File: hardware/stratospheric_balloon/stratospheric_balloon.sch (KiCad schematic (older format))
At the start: 6 parts

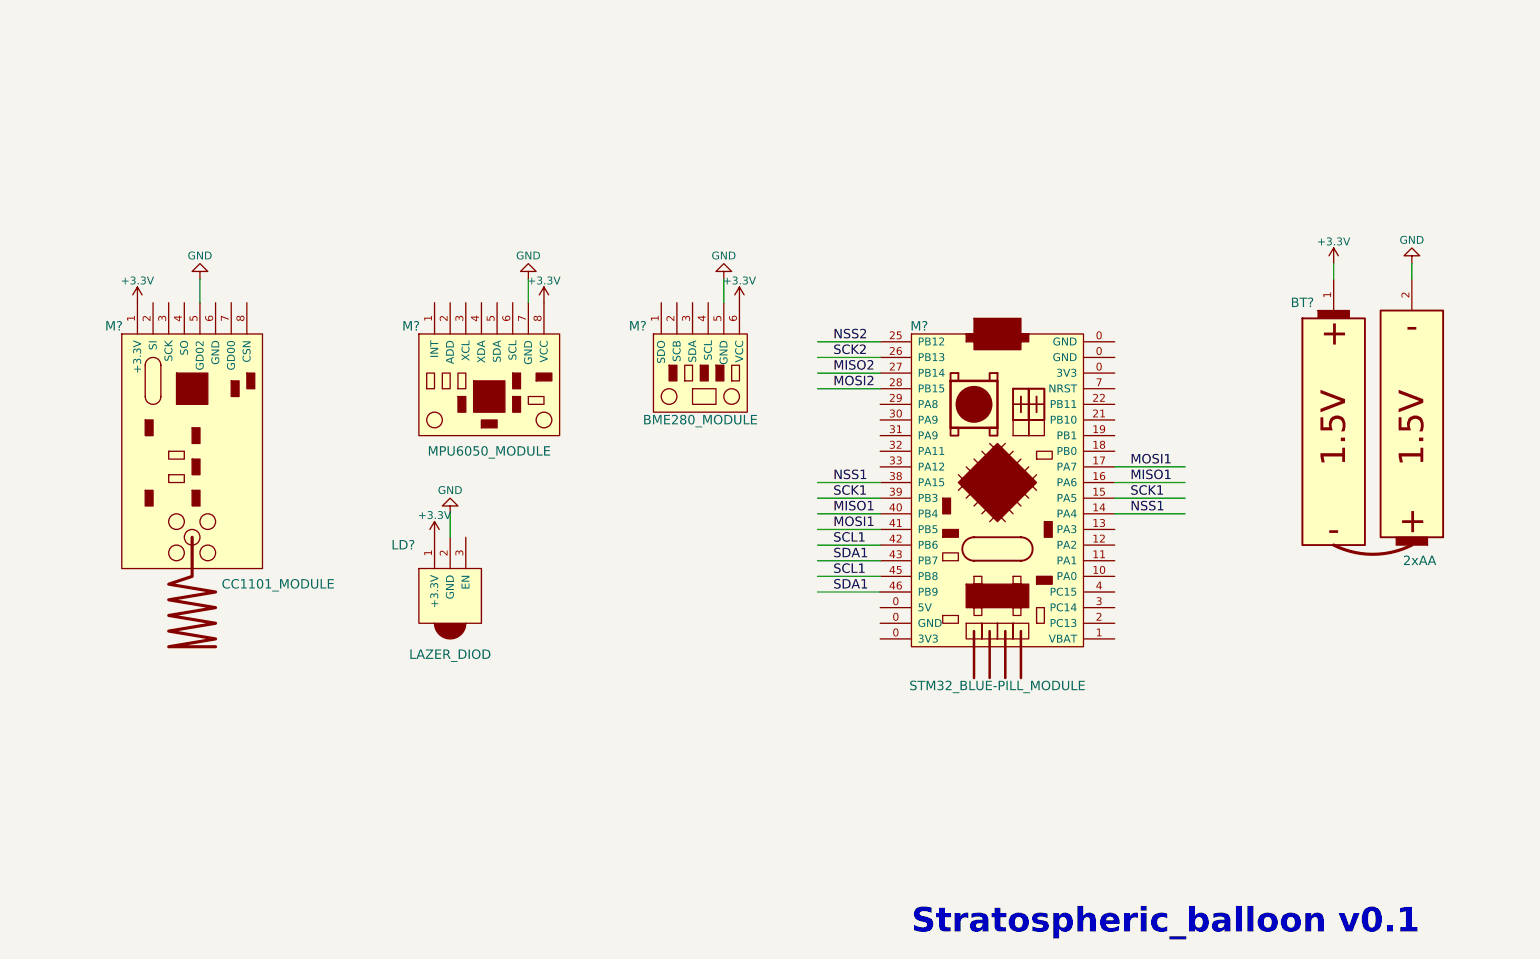
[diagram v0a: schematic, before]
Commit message: Schematic diagram was corrected
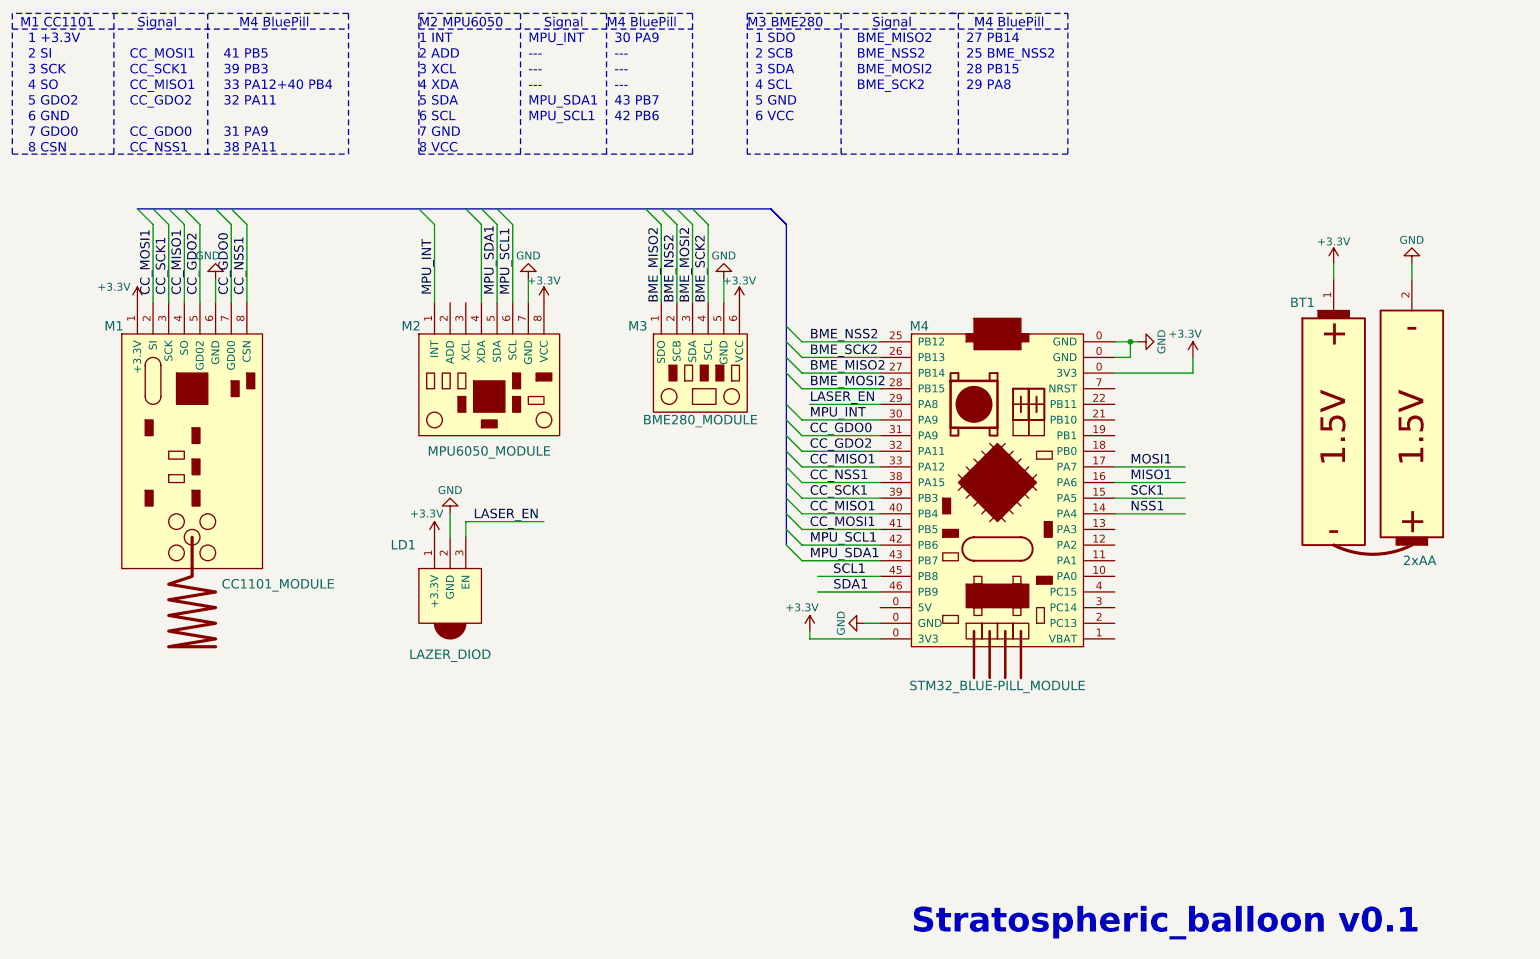
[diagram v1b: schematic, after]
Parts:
- gave numbers to parts that had none: 6
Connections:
- net labels added: BME_MISO2, BME_MOSI2, BME_NSS2, BME_SCK2, CC_GDO0, CC_GDO2, CC_MISO1, CC_MOSI1, CC_NSS1, CC_SCK1, LASER_EN, MPU_INT, MPU_SCL1, MPU_SDA1
- net labels removed: MISO2, MOSI2, NSS2, SCK2
- wire segments 26 -> 55
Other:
- note added: "---"
- note added: "1 +3.3V"
- note added: "1 INT"
- note added: "1 SDO"
- note added: "2 ADD"
- note added: "2 SCB"
- note added: "2 SI"
- note added: "25 BME_NSS2"
- note added: "27 PB14"
- note added: "28 PB15"
- note added: "29 PA8"
- note added: "3 SCK"
- note added: "3 SDA"
- note added: "3 XCL"
- note added: "30 PA9"
- note added: "31 PA9"
- note added: "32 PA11"
- note added: "33 PA12+40 PB4"
- note added: "38 PA11"
- note added: "39 PB3"
- note added: "4 SCL"
- note added: "4 SO"
- note added: "4 XDA"
- note added: "41 PB5"
- note added: "42 PB6"
- note added: "43 PB7"
- note added: "5 GDO2"
- note added: "5 GND"
- note added: "5 SDA"
- note added: "6 GND"
- note added: "6 SCL"
- note added: "6 VCC"
- note added: "7 GDO0"
- note added: "7 GND"
- note added: "8 CSN"
- note added: "8 VCC"
- note added: "BME_MISO2"
- note added: "BME_MOSI2"
- note added: "BME_NSS2"
- note added: "BME_SCK2"
- note added: "CC_GDO0"
- note added: "CC_GDO2"
- note added: "CC_MISO1"
- note added: "CC_MOSI1"
- note added: "CC_NSS1"
- note added: "CC_SCK1"
- note added: "M1 CC1101"
- note added: "M2 MPU6050"
- note added: "M3 BME280"
- note added: "M4 BluePill"
- note added: "MPU_INT"
- note added: "MPU_SCL1"
- note added: "MPU_SDA1"
- note added: "Signal"
